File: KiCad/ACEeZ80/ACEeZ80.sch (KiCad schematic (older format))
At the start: 58 parts, among them X2 20MHz

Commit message: Remove some old versions correct logic on ACE3NOKB.
Signed-off-by: John Bradley <flypie@rocketmail.com>
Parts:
- added Logo?: ZilogBack, Symbol:ZilogInsideBack, symbol Graphic:ZilogBack
- added Logo?: ZilogFront, Symbol:ZilogInsideFront, symbol Graphic:ZilogFront
- C10, C13, C14, C15, C16, C17, C18, C19, C20, C21, C405, C406, C407, C408, C409: footprint Capacitor_THT:C_Disc_D5.0mm_W2.5mm_P5.00mm -> K104K10X7RF53H5; Description Vishay 100nF Multilayer Ceramic Capacitor MLCC 50V dc +~-10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 -> Vishay 100nF Multilayer Ceramic Capacitor MLCC 50V dc +/-10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; RS Price/Stock http:~/uk.rs-online.com/web/p/products/8523267 -> http://uk.rs-online.com/web/p/products/8523267
- POWER-9V-DC1: Field4 https:~/www.digikey.co.uk/product-detail/en/cui-inc/PJ-036C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 -> https://www.digikey.co.uk/product-detail/en/cui-inc/PJ-036C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; Field9 https:~/www.cui.com/product/interconnect/connectors/dc-powe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 -> https://www.cui.com/product/interconnect/connectors/dc-powe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
- Z0: value Z80-182-L182-VQFP-100 -> Z80F91; footprint Package_QFP:VQFP-100_14x14mm_P0.5mm -> Package_QFP:LQFP-144_20x20mm_P0.5mm; symbol Zilog_Z180:Z80-182-L182-VQFP-100 -> Zilog_eZ80:eZ80F91-LQFP; Description Zilog Z80182 & Z8L182, Z80 Microprocessor Z180 8bit CISC 10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 -> 8-bit Microcontrollers - MCU 50MHz 0KB Flash 0KB SRAM 3.5V; Height 2.8 -> 1.6; Manufacturer_Part_Number Z8018233FSG -> EZ80L92AZ050EG
- Z1-2: footprint Package_DIP:DIP-28_W15.24mm -> Package_DIP:DIP-28_W15.24mm_Socket; Description (none) -> AT28C256-15PU, Parallel EEPROM Memory 256kbit, Parallel, 15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; Height (none) -> 4.826; Manufacturer_Name (none) -> Microchip; Manufacturer_Part_Number (none) -> AT28C256-15PU; Mouser Part Number (none) -> 556-AT28C25615PU; Mouser Price/Stock (none) -> https://www.mouser.com/Search/Refine.aspx?Keyword=556-AT28C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; RS Part Number (none) -> 1276570P; RS Price/Stock (none) -> http://uk.rs-online.com/web/p/products/1276570P
- Z3-4: Mouser Price/Stock https:~/www.mouser.com/Search/Refine.aspx?Keyword=913-AS6C8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 -> https://www.mouser.com/Search/Refine.aspx?Keyword=913-AS6C8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; RS Price/Stock https:~/uk.rs-online.com/web/p/products/1700737 -> https://uk.rs-online.com/web/p/products/1700737
- Z80CPUOUT1: value Conn_02x22_Odd_Even -> Conn_02x24_Odd_Even; symbol Connector_Generic:Conn_02x22_Odd_Even -> Connector_Generic:Conn_02x24_Odd_Even
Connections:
- net labels added: +BATT, -BATT, A20, A21, A22, A23, COL, CRS, I2C-Clock, I2C-Data, MDC, MDIO, PB7, RxD0, RxD1, RxD2, RxD3, Rx_CLK, Rx_DV, Rx_ER, TxD0, TxD1, TxD2, TxD3, TxEN, Tx_CLK, Tx_ER
- net labels removed: CKA0, CKA1, E, ST, ~INT0, ~INT1, ~INT2, ~RFSH
- wire segments 415 -> 463
- no-connect marks 22 -> 29
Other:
- note added: "Z51F0811 MCU"
- moved on the sheet: C100, C101, C7, R25, X2

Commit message: Tidy up Capcitors in power supply to remove errors add labels.
Primary Development is now ACE3NOKB.


Signed-off-by: John Bradley <flypie@rocketmail.com>
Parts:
- removed Z3-4: AS6C8008-55ZIN, Package_SO:TSOP-II-44_10.16x18.41mm_P0.8mm, symbol Memory_RAM:AS6C8008-55ZIN
- added D406, D407, D408: 1N4148, Diode_THT:D_DO-35_SOD27_P2.54mm_Vertical_AnodeUp, symbol Diode:1N4148
- added Z3-4: AS7C316096A-10TIN, Package_SO:TSOP-I-48_18.4x12mm_P0.5mm, symbol SamacSys_Parts:AS7C316096A-10TIN
- C10, C13, C14, C15, C16, C17, C18, C19, C20, C21, C405, C406, C407, C408, C409: footprint K104K10X7RF53H5 -> Capacitor_THT:C_Disc_D3.0mm_W2.0mm_P2.50mm; symbol SamacSys_Parts:K104K10X7RF53H5 -> Device:C
- Z1-2: symbol Memory_EEPROM:AT28C256-15PU -> Memory_EEPROM:28C256
- Z80CPUOUT1: footprint Connector_PinHeader_2.54mm:PinHeader_2x22_P2.54mm_Vertical -> Connector_PinHeader_2.54mm:PinHeader_2x24_P2.54mm_Vertical
- gave numbers to parts that had none: 2
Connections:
- net labels removed: CKS
- wire segments 463 -> 470
- no-connect marks 29 -> 31
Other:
- moved on the sheet: D400, D401, D402, D403, D404, D405, Logo1, Logo2, R420

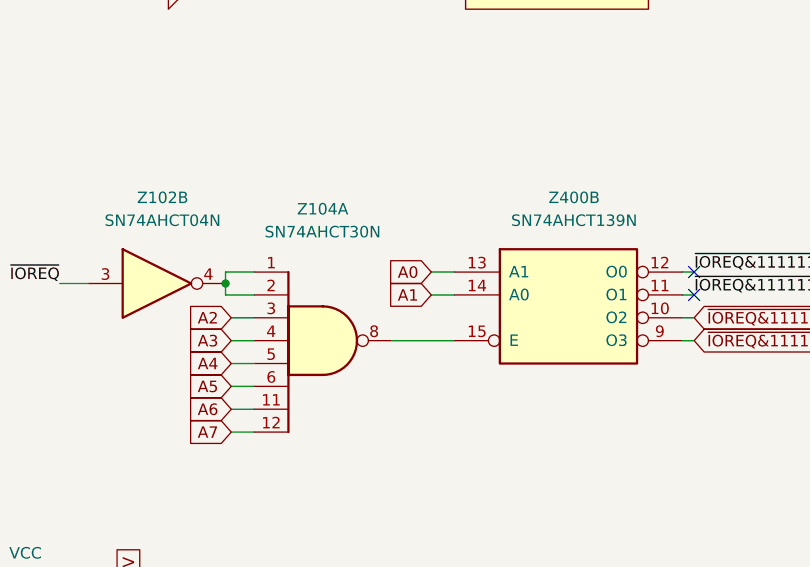
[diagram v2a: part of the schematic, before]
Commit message: Fix mistake on 74ALS166 Z28 connection clock connected to wrong pin. Add KeyBoard Project. Adjust resitor physical size.
Signed-off-by: John Bradley <flypie@rocketmail.com>
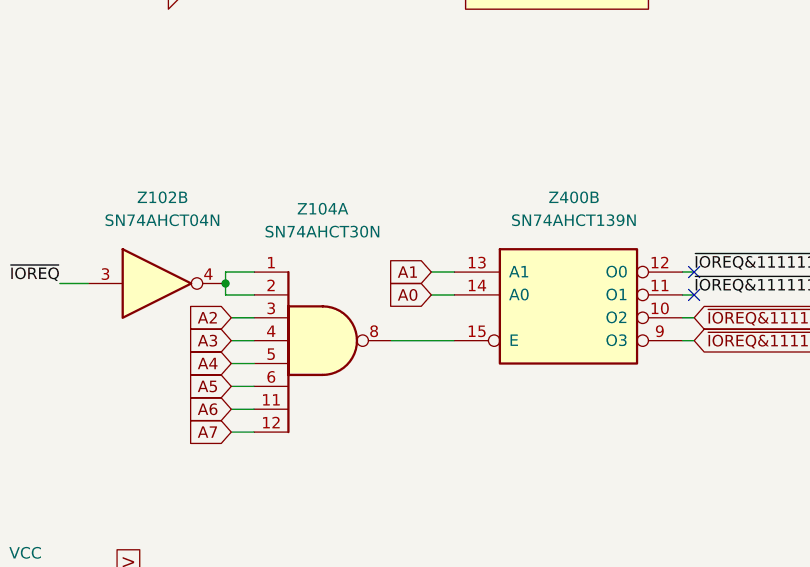
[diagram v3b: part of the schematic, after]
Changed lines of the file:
@@
 	8000 9725 8100 9725
 Wire Wire Line
-	8975 9025 8875 9025
+	8975 9125 8875 9125
 Text GLabel 8000 9725 0    50   Input ~ 0
 A7
@@
 A3
 Wire Wire Line
-	8975 9125 8875 9125
+	8975 9025 8875 9025
 Wire Wire Line
 	8100 9625 8000 9625
@@
 F1 "Tape&SPKR.sch" 125
 $EndSheet
+Text GLabel 8875 9125 0    50   Input ~ 0
+A0
 Text GLabel 8875 9025 0    50   Input ~ 0
-A0
-Text GLabel 8875 9125 0    50   Input ~ 0
 A1
 Text GLabel 9800 1275 0    50   Input ~ 0

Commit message: Double check transistors
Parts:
- renumbered Z100 to Z29
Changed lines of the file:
@@
 	8825 6975 8725 6975
 $Comp
-L 74xx:74LS138 Z100
+L 74xx:74LS138 Z29
 U 1 1 5F80C8A4
 P 3500 3425
-F 0 "Z100" H 3500 4250 50  0000 C CNN
+F 0 "Z29" H 3500 4250 50  0000 C CNN
 F 1 "SN74AHCT138N" H 3500 4150 50  0000 C CNN
 F 2 "Package_DIP:DIP-16_W7.62mm" H 3500 3425 50  0001 C CNN

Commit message: Update Post ACE4 Boards. Add MPU to eZ80 for Keyboard. Add eZ80 RAM card. Split MMU and PSU into own sub-schema.
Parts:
- removed C10, C13, C14, C15, C16, C17, C18, C19, C20, C21, C405, C406, C407, C408, C409: 100nf, Capacitor_THT:C_Disc_D3.0mm_W2.0mm_P2.50mm, symbol Device:C
- removed C11: 100uf, Capacitor_THT:CP_Radial_D4.0mm_P1.50mm, symbol Device:CP
- removed C12: 100uf, Capacitor_THT:CP_Radial_D5.0mm_P2.00mm, symbol Device:CP
- removed C9: 100u, Capacitor_THT:CP_Radial_D5.0mm_P2.00mm, symbol Device:CP
- removed D406, D407: 1N4148, Diode_THT:D_DO-35_SOD27_P2.54mm_Vertical_AnodeUp, symbol Diode:1N4148
- removed L1: 100 nH, Inductor_THT:L_Axial_L13.0mm_D4.5mm_P5.08mm_Vertical_Fastron_HCCC, symbol Device:L
- removed LVR1: LM7805_TO220, Package_TO_SOT_THT:TO-220-3_Vertical, symbol Regulator_Linear:LM7805_TO220
- removed POWER-9V-DC1: PJ-036C, cuipj:CUI_PJ-036C, symbol PJ-036C:PJ-036C
- removed Z10, Z11, Z9: SN74AHCT393N, Package_DIP:DIP-14_W7.62mm, symbol 74xx:74LS393
- removed unit 7 of Z102
- removed unit 2 of Z104
- removed Z19: SN74AHCT00N, Package_DIP:DIP-14_W7.62mm, symbol 74xx:74HCT00
- removed Z20: SN74AHCT08N, Package_DIP:DIP-14_W7.62mm, symbol 74xx:74LS08
- removed Z21, Z22: SN74AHCT11N, Package_DIP:DIP-14_W7.62mm, symbol 74xx:74LS11
- removed Z23: SN74AHCT86N, Package_DIP:DIP-14_W7.62mm, symbol 74xx:74LS86
- removed Z24, Z25: SN74AHCT02N, Package_DIP:DIP-14_W7.62mm, symbol 74xx:74HCT02
- removed Z27: SN74AHCT74N, Package_DIP:DIP-14_W7.62mm, symbol 74xx:74LS74
- removed unit 2 of Z303
- added D409: 1N4148, Diode_THT:D_DO-35_SOD27_P2.54mm_Vertical_AnodeUp, symbol Diode:1N4148
- added J1: Connector_Generic:Conn_02x20_Odd_Even, Connector_PinSocket_1.27mm:PinSocket_2x20_P1.27mm_Vertical, symbol Connector_Generic:Conn_02x20_Odd_Even
- added Z1: SN74AHCT138N, Package_DIP:DIP-16_W7.62mm, symbol 74xx:74LS138
- Z0: value Z80F91 -> eZ80F91
- Z1-2: value 28C256 -> SST39SF010-LCC; footprint Package_DIP:DIP-28_W15.24mm_Socket -> Package_LCC:PLCC-32_THT_Socket_11.4x14.0mm_P1.27mm; symbol Memory_EEPROM:28C256 -> Memory_Flash:SST39SF010-LCC; Description AT28C256-15PU, Parallel EEPROM Memory 256kbit, Parallel, 15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 -> (none); Height 4.826 -> (none); Manufacturer_Name Microchip -> (none); Manufacturer_Part_Number AT28C256-15PU -> (none)
- Z104, Z303: footprint Package_DIP:DIP-14_W7.62mm -> Package_SO:SOIC-14_3.9x8.7mm_P1.27mm
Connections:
- net labels added: ~1&2Meg, ~11&12Meg, ~13&14Meg, ~15&16Meg, ~3&4Meg, ~5&6Meg, ~7&8Meg, ~9&10Meg
- net labels removed: +9V, -BATT, RxS\~CTS~, TRxCA, TRxCB, TxS, ~DTR~\REQA, ~RTxCA, ~RTxCB, ~SYNCA, ~SYNCB, ~W~\REQA
- wire segments 470 -> 394
- no-connect marks 31 -> 28
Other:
- moved on the sheet: Z102A, Z29, Z303A

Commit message: Add some outline designs for add on cards and adapters. Modify ACEeZ80 so that full address bus is on the expander slot, add I2C pins
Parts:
- added I2COUT1: Conn_02x01_Odd_Even, Connector_PinHeader_2.54mm:PinHeader_2x01_P2.54mm_Vertical, symbol Connector_Generic:Conn_02x01
- added unit 3 of Z102
- added Z19: SN74AHCT00N, Package_DIP:DIP-14_W7.62mm, symbol 74xx:74LS00
- added Z22: SN74AHCT11N, Package_DIP:DIP-14_W7.62mm, symbol 74xx:74LS11
- added Z23: SN74AHCT86N, Package_DIP:DIP-14_W7.62mm, symbol 74xx:74LS86
- added Z25: SN74AHCT02N, Package_DIP:DIP-14_W7.62mm, symbol 74xx:74LS02
- X2: value 20MHz -> 50MHz
- Z80CPUOUT1: value Conn_02x24_Odd_Even -> Conn_02x26_Odd_Even; footprint Connector_PinHeader_2.54mm:PinHeader_2x24_P2.54mm_Vertical -> Connector_PinHeader_2.54mm:PinHeader_2x26_P2.54mm_Vertical; symbol Connector_Generic:Conn_02x24_Odd_Even -> Connector_Generic:Conn_02x26_Odd_Even
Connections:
- net A16: now also Z80CPUOUT1.45 (Pin_45)
- net A17: now also Z80CPUOUT1.47 (Pin_47)
- net A18: now also Z80CPUOUT1.49 (Pin_49)
- net A19: now also Z80CPUOUT1.51 (Pin_51)
- net A20: now also Z80CPUOUT1.52 (Pin_52); no longer Z80CPUOUT1.45 (Pin_45)
- net A21: now also Z80CPUOUT1.50 (Pin_50); no longer Z80CPUOUT1.47 (Pin_47)
- net A22: now also Z80CPUOUT1.48 (Pin_48); no longer Z80CPUOUT1.46 (Pin_46)
- net A23: now also Z80CPUOUT1.46 (Pin_46); no longer Z80CPUOUT1.48 (Pin_48)
- net I2C-Clock: now also I2COUT1.1 (Pin_1)
- net I2C-Data: now also I2COUT1.2 (Pin_2)
- no-connect marks 28 -> 49
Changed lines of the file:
@@
 $EndComp
 NoConn ~ 10500 2075
+Text GLabel 10500 3475 2    50   Input ~ 0
+A23
 Text GLabel 10500 3575 2    50   Input ~ 0
-A23
-Text GLabel 10500 3475 2    50   Input ~ 0
 A22
 Wire Wire Line
+	10400 3575 10500 3575
+Wire Wire Line
 	10400 3475 10500 3475
-Wire Wire Line
-	10400 3575 10500 3575
-Text GLabel 9800 3475 0    50   Input ~ 0
+Text GLabel 10500 3775 2    50   Input ~ 0
 A20
-Text GLabel 9800 3575 0    50   Input ~ 0
+Text GLabel 10500 3675 2    50   Input ~ 0
 A21
 Wire Wire Line
-	9900 3575 9800 3575
-Wire Wire Line
-	9900 3475 9800 3475
+	10400 3675 10500 3675
+Wire Wire Line
+	10400 3775 10500 3775
 Text GLabel 10500 2175 2    50   Input ~ 0
 ~M1
@@
 U 1 1 604B268F
 P 5850 7275
-F 0 "X2" H 5925 7625 59  0000 C CNN
-F 1 "20MHz" H 5925 7475 59  0000 C CNN
+F 0 "X2" V 5775 7425 59  0000 L CNN
+F 1 "50MHz" V 5875 7425 59  0000 L CNN
 F 2 "Crystal:Crystal_HC49-U_Vertical" H 5850 7275 50  0001 C CNN
 F 3 "~" H 5850 7275 50  0001 C CNN
@@
 DA0
 $Comp
-L Connector_Generic:Conn_02x24_Odd_Even Z80CPUOUT1
+L Connector_Generic:Conn_02x26_Odd_Even Z80CPUOUT1
 U 1 1 5F80C84A
-P 10100 2375
-F 0 "Z80CPUOUT1" H 10175 3815 50  0000 C CNN
-F 1 "Conn_02x24_Odd_Even" H 10175 3715 50  0000 C CNN
-F 2 "Connector_PinHeader_2.54mm:PinHeader_2x24_P2.54mm_Vertical" H 10100 2375 50  0001 C CNN
-F 3 "~" H 10100 2375 50  0001 C CNN
-	1    10100 2375
+P 10100 2475
+F 0 "Z80CPUOUT1" H 10175 3915 50  0000 C CNN
+F 1 "Conn_02x26_Odd_Even" H 10175 3815 50  0000 C CNN
+F 2 "Connector_PinHeader_2.54mm:PinHeader_2x26_P2.54mm_Vertical" H 10100 2475 50  0001 C CNN
+F 3 "~" H 10100 2475 50  0001 C CNN
+	1    10100 2475
 	1    0    0    -1
 $EndComp
@@
 Text Label 2225 3775 0    50   ~ 0
 ~15&16Meg
+Text GLabel 9800 3775 0    50   Input ~ 0
+A19
+Text GLabel 9800 3675 0    50   Input ~ 0
+A18
+Wire Wire Line
+	9900 3675 9800 3675
+Wire Wire Line
+	9900 3775 9800 3775
+Text GLabel 9800 3475 0    50   Input ~ 0
+A16
+Text GLabel 9800 3575 0    50   Input ~ 0
+A17
+Wire Wire Line
+	9900 3575 9800 3575
+Wire Wire Line
+	9900 3475 9800 3475
+$Comp
+L Connector_Generic:Conn_02x01 I2COUT1
+U 1 1 5DFB669B
+P 10125 4225
+F 0 "I2COUT1" H 10175 4500 50  0000 C CNN
+F 1 "Conn_02x01_Odd_Even" H 10175 4400 50  0000 C CNN
+F 2 "Connector_PinHeader_2.54mm:PinHeader_2x01_P2.54mm_Vertical" H 10125 4225 50  0001 C CNN
+F 3 "~" H 10125 4225 50  0001 C CNN
+	1    10125 4225
+	1    0    0    -1
+$EndComp
+Text GLabel 9875 4225 0    50   Input ~ 0
+I2C-Clock
+Wire Wire Line
+	9925 4225 9875 4225
+Text GLabel 10475 4225 2    50   Input ~ 0
+I2C-Data
+Wire Wire Line
+	10425 4225 10475 4225
+$Comp
+L 74xx:74HCT04 Z?
+U 3 1 5DCA9869
+P -500 10300
+AR Path="/5D66C06C/5DCA9869" Ref="Z?"  Part="5"
+AR Path="/5DCA9869" Ref="Z102"  Part="3"
+F 0 "Z102" H -500 10650 50  0000 C CNN
+F 1 "SN74AHCT04N" H -500 10550 50  0000 C CNN
+F 2 "Package_DIP:DIP-14_W7.62mm" H -500 10300 50  0001 C CNN
+F 3 "https://assets.nexperia.com/documents/data-sheet/74HC_HCT04.pdf" H -500 10300 50  0001 C CNN
+	3    -500 10300
+	1    0    0    -1
+$EndComp
+NoConn ~ -200 10300
+NoConn ~ -800 10300
+$Comp
+L 74xx:74LS86 Z?
+U 1 1 5DD56C70
+P -500 10800
+AR Path="/5EED81F4/5DD56C70" Ref="Z?"  Part="5"
+AR Path="/5DD56C70" Ref="Z23"  Part="1"
+F 0 "Z23" H -500 10450 50  0000 C CNN
+F 1 "SN74AHCT86N" H -500 10550 50  0000 C CNN
+F 2 "Package_DIP:DIP-14_W7.62mm" H -500 10800 50  0001 C CNN
+F 3 "74xx/74ls86.pdf" H -500 10800 50  0001 C CNN
+	1    -500 10800
+	1    0    0    1
+$EndComp
+NoConn ~ -800 10900
+NoConn ~ -800 10700
+NoConn ~ -200 10800
+$Comp
+L 74xx:74LS86 Z?
+U 2 1 5DE1C1C3
+P -500 11200
+AR Path="/5EED81F4/5DE1C1C3" Ref="Z?"  Part="5"
+AR Path="/5DE1C1C3" Ref="Z23"  Part="2"
+F 0 "Z23" H -500 11450 50  0000 C CNN
+F 1 "SN74AHCT86N" H -500 11550 50  0000 C CNN
+F 2 "Package_DIP:DIP-14_W7.62mm" H -500 11200 50  0001 C CNN
+F 3 "74xx/74ls86.pdf" H -500 11200 50  0001 C CNN
+	2    -500 11200
+	1    0    0    1
+$EndComp
+NoConn ~ -800 11300
+NoConn ~ -800 11100
+NoConn ~ -200 11200
+$Comp
+L 74xx:74LS00 Z?
+U 3 1 5DE54CA9
+P -525 12075
+AR Path="/5EED81F4/5DE54CA9" Ref="Z?"  Part="5"
+AR Path="/5DE54CA9" Ref="Z19"  Part="3"
+F 0 "Z19" H -525 11700 50  0000 C CNN
+F 1 "SN74AHCT00N" H -525 11800 50  0000 C CNN
+F 2 "Package_DIP:DIP-14_W7.62mm" H -525 12075 50  0001 C CNN
+F 3 "http://www.ti.com/lit/gpn/sn74ls00" H -525 12075 50  0001 C CNN
+	3    -525 12075
+	1    0    0    1
+$EndComp
+NoConn ~ -825 12175
+NoConn ~ -825 11975
+NoConn ~ -225 12075
+$Comp
+L 74xx:74LS00 Z?
+U 4 1 5DF1B68B
+P -525 12750
+AR Path="/5EED81F4/5DF1B68B" Ref="Z?"  Part="5"
+AR Path="/5DF1B68B" Ref="Z19"  Part="4"
+F 0 "Z19" H -525 12400 50  0000 C CNN
+F 1 "SN74AHCT00N" H -525 12500 50  0000 C CNN
+F 2 "Package_DIP:DIP-14_W7.62mm" H -525 12750 50  0001 C CNN
+F 3 "http://www.ti.com/lit/gpn/sn74ls00" H -525 12750 50  0001 C CNN
+	4    -525 12750
+	1    0    0    1
+$EndComp
+NoConn ~ -825 12850
+NoConn ~ -825 12650
+NoConn ~ -225 12750
+$Comp
+L 74xx:74LS11 Z?
+U 3 1 5DF56F8E
+P -525 13400
+AR Path="/5EED81F4/5DF56F8E" Ref="Z?"  Part="4"
+AR Path="/5DF56F8E" Ref="Z22"  Part="3"
+F 0 "Z22" H -525 13050 50  0000 C CNN
+F 1 "SN74AHCT11N" H -525 13150 50  0000 C CNN
+F 2 "Package_DIP:DIP-14_W7.62mm" H -525 13400 50  0001 C CNN
+F 3 "http://www.ti.com/lit/gpn/sn74LS11" H -525 13400 50  0001 C CNN
+	3    -525 13400
+	1    0    0    1
+$EndComp
+NoConn ~ -825 13300
+NoConn ~ -825 13400
+NoConn ~ -825 13500
+NoConn ~ -225 13400
+$Comp
+L 74xx:74LS02 Z?
+U 3 1 5E0B9D8F
+P -525 14075
+AR Path="/5EED81F4/5E0B9D8F" Ref="Z?"  Part="5"
+AR Path="/5E0B9D8F" Ref="Z25"  Part="3"
+F 0 "Z25" H -525 13700 50  0000 C CNN
+F 1 "SN74AHCT02N" H -525 13800 50  0000 C CNN
+F 2 "Package_DIP:DIP-14_W7.62mm" H -525 14075 50  0001 C CNN
+F 3 "http://www.ti.com/lit/gpn/sn74ls02" H -525 14075 50  0001 C CNN
+	3    -525 14075
+	1    0    0    1
+$EndComp
+NoConn ~ -825 14175
+NoConn ~ -825 13975
+NoConn ~ -225 14075
 $EndSCHEMATC

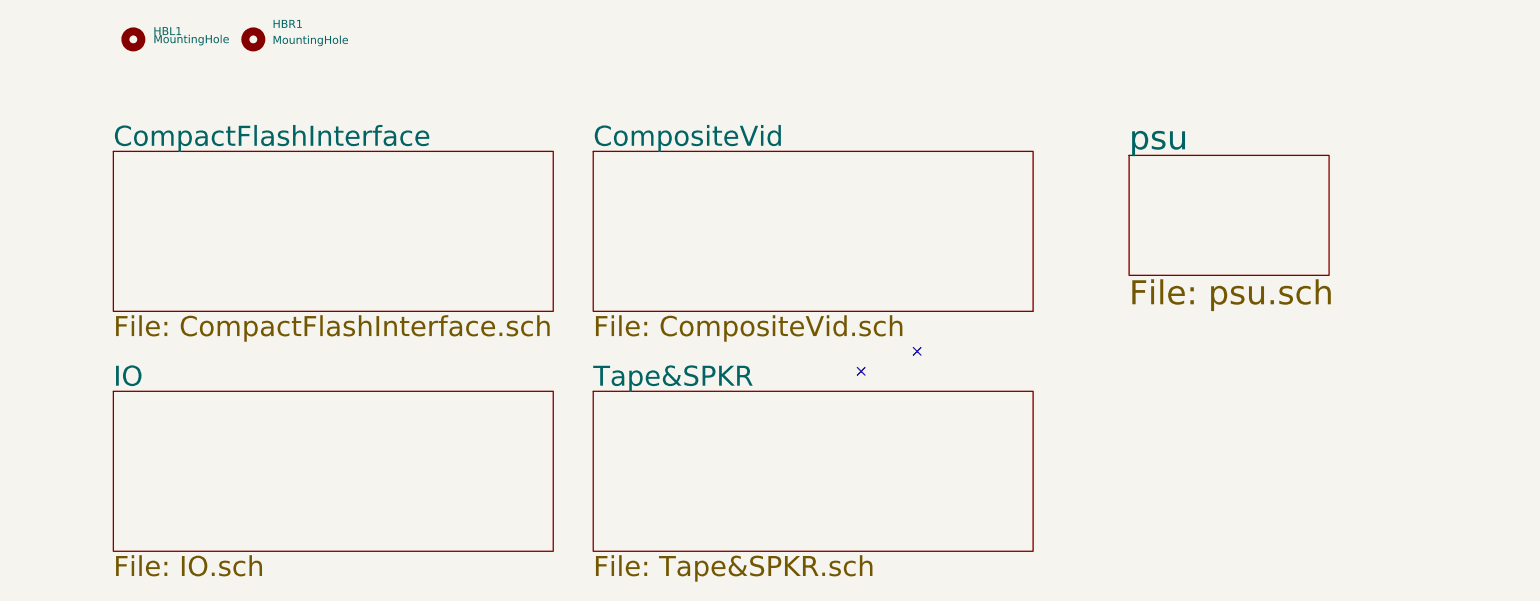
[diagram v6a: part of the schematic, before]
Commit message: Add example to UniBoard. Correct power and bus routing on ACEeZ80.jpg
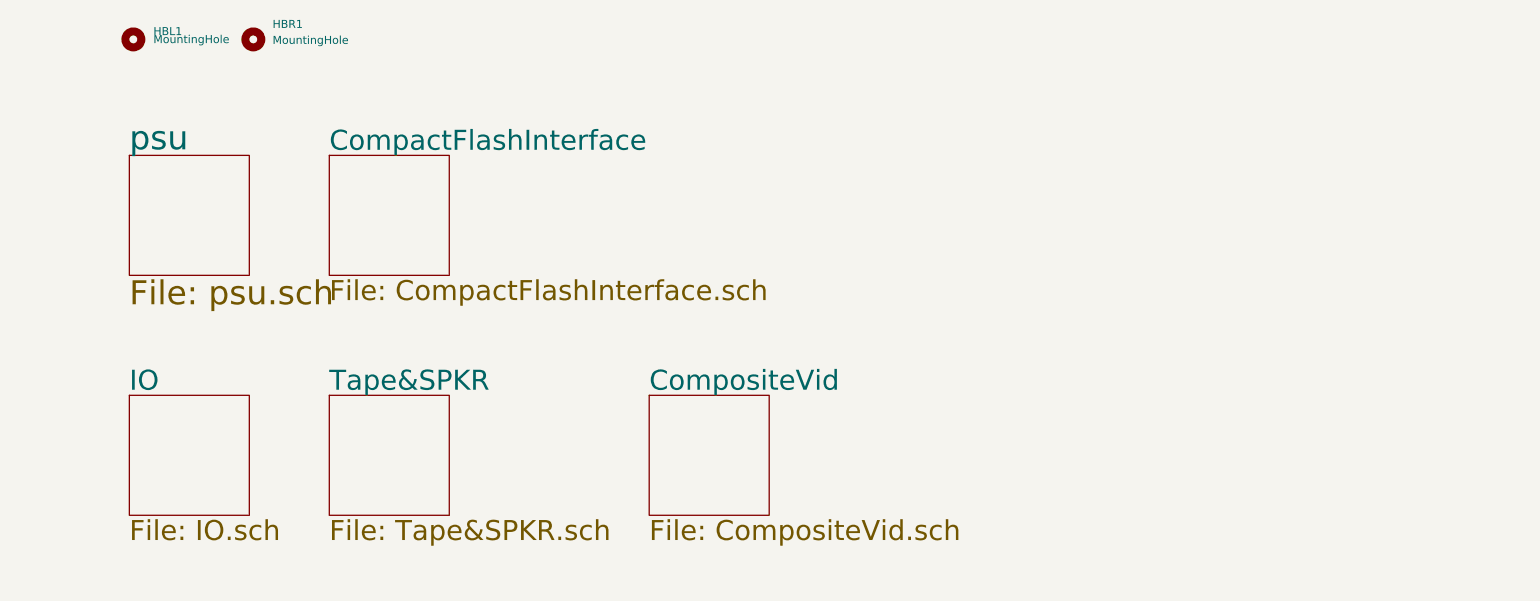
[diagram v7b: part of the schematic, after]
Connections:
- no-connect marks 49 -> 47
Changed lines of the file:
@@
 NoConn ~ 1600 4525
 $Sheet
-S 7250 13250 1250 750
+S 1000 13250 750  750
 U 5EED81F4
 F0 "psu" 150
@@
 	4300 1175 4200 1175
 $Sheet
-S 900  14725 2750 1000
+S 1000 14750 750  750
 U 5D9DD1F0
 F0 "IO" 125
@@
 A0
 $Sheet
-S 3900 14725 2750 1000
+S 2250 14750 750  750
 U 5D66C06C
 F0 "Tape&SPKR" 125
@@
 Wire Wire Line
 	8000 9725 8100 9725
-NoConn ~ 5575 14600
 $Comp
 L 74xx:74LS30 Z303
@@
 	5775 3625 5875 3625
 $Sheet
-S 3900 13225 2750 1000
+S 4250 14750 750  750
 U 5FA4DA0E
 F0 "CompositeVid" 125
@@
 A11
 $Sheet
-S 900  13225 2750 1000
+S 2250 13250 750  750
 U 5EDE0D3D
 F0 "CompactFlashInterface" 125
@@
 Wire Wire Line
 	4775 3325 4675 3325
-NoConn ~ 5925 14475
 $Comp
 L power:VCC #~~~PWR0127
